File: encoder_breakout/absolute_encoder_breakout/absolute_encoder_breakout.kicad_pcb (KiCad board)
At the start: 2 copper layers, 14.3 x 9.7 mm, 2 parts

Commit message: Fix Breakout Board
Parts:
- moved U1 1.27 mm to (139.7, 75.2), turned to -90 degrees
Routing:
- net Net-(U1-OUT): track 5.43 -> 9.35 mm, vias 0 -> 1
- net Net-(U1-VDD3V3): track 5.74 -> 8.15 mm
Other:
- board size 14.3 x 9.7 mm -> 12 x 9.7 mm
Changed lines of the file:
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@@
 	(footprint "Package_SO:SOIC-8_3.9x4.9mm_P1.27mm"
 		(layer "F.Cu")
-		(at 138.43 75.15 180)
+		(at 139.7 75.184 -90)
 		(descr "SOIC, 8 Pin (JEDEC MS-012AA, https://www.analog.com/media/en/package-pcb-resources/package/pkg_pdf/soic_narrow-r/r_8.pdf), generated with kicad-footprint-generator ipc_gullwing_generator.py")
 		(tags "SOIC SO")
 		(property "Reference" "U1"
-			(at 0 -3.4 0)
-			(layer "F.SilkS")
+			(at 4.318 0 180)
+			(layer "F.SilkS")
+			(effects
+				(font
+					(size 0.635 0.635)
+					(thickness 0.15)
+				)
+			)
+		)
+		(property "Value" "~"
+			(at 0 3.4 90)
+			(layer "F.Fab")
 			(effects
 				(font
@@
 			)
 		)
-		(property "Value" "~"
-			(at 0 3.4 0)
-			(layer "F.Fab")
-			(effects
-				(font
-					(size 1 1)
-					(thickness 0.15)
-				)
-			)
-		)
 		(property "Datasheet" "https://look.ams-osram.com/m/7059eac7531a86fd/original/AS5600-DS000365.pdf"
-			(at 0 0 0)
+			(at 0 0 90)
 			(layer "F.Fab")
 			(hide yes)
@@
 		)
 		(property "Description" ""
-			(at 0 0 0)
+			(at 0 0 90)
 			(layer "F.Fab")
 			(hide yes)
@@
 		(fp_line
 			(start 0 2.56)
+			(end -1.95 2.56)
+			(stroke
+				(width 0.12)
+				(type solid)
+			)
+			(layer "F.SilkS")
+		)
+		(fp_line
+			(start 0 2.56)
 			(end 1.95 2.56)
 			(stroke
@@
 		)
 		(fp_line
-			(start 0 2.56)
-			(end -1.95 2.56)
+			(start 0 -2.56)
+			(end -1.95 -2.56)
 			(stroke
 				(width 0.12)
@@
 			(start 0 -2.56)
 			(end 1.95 -2.56)
-			(stroke
-				(width 0.12)
-				(type solid)
-			)
-			(layer "F.SilkS")
-		)
-		(fp_line
-			(start 0 -2.56)
-			(end -1.95 -2.56)
 			(stroke
 				(width 0.12)
@@
 		)
 		(fp_line
+			(start -2.2 2.7)
+			(end -2.2 2.46)
+			(stroke
+				(width 0.05)
+				(type solid)
+			)
+			(layer "F.CrtYd")
+		)
+		(fp_line
+			(start 2.2 2.7)
+			(end -2.2 2.7)
+			(stroke
+				(width 0.05)
+				(type solid)
+			)
+			(layer "F.CrtYd")
+		)
+		(fp_line
+			(start -3.7 2.46)
+			(end -3.7 -2.46)
+			(stroke
+				(width 0.05)
+				(type solid)
+			)
+			(layer "F.CrtYd")
+		)
+		(fp_line
+			(start -2.2 2.46)
+			(end -3.7 2.46)
+			(stroke
+				(width 0.05)
+				(type solid)
+			)
+			(layer "F.CrtYd")
+		)
+		(fp_line
+			(start 2.2 2.46)
+			(end 2.2 2.7)
+			(stroke
+				(width 0.05)
+				(type solid)
+			)
+			(layer "F.CrtYd")
+		)
+		(fp_line
 			(start 3.7 2.46)
 			(end 2.2 2.46)
@@
 		)
 		(fp_line
+			(start -3.7 -2.46)
+			(end -2.2 -2.46)
+			(stroke
+				(width 0.05)
+				(type solid)
+			)
+			(layer "F.CrtYd")
+		)
+		(fp_line
+			(start -2.2 -2.46)
+			(end -2.2 -2.7)
+			(stroke
+				(width 0.05)
+				(type solid)
+			)
+			(layer "F.CrtYd")
+		)
+		(fp_line
+			(start 2.2 -2.46)
+			(end 3.7 -2.46)
+			(stroke
+				(width 0.05)
+				(type solid)
+			)
+			(layer "F.CrtYd")
+		)
+		(fp_line
 			(start 3.7 -2.46)
 			(end 3.7 2.46)
@@
 		)
 		(fp_line
-			(start 2.2 2.7)
-			(end -2.2 2.7)
-			(stroke
-				(width 0.05)
-				(type solid)
-			)
-			(layer "F.CrtYd")
-		)
-		(fp_line
-			(start 2.2 2.46)
-			(end 2.2 2.7)
-			(stroke
-				(width 0.05)
-				(type solid)
-			)
-			(layer "F.CrtYd")
-		)
-		(fp_line
-			(start 2.2 -2.46)
-			(end 3.7 -2.46)
+			(start -2.2 -2.7)
+			(end 2.2 -2.7)
 			(stroke
 				(width 0.05)
@@
 			(start 2.2 -2.7)
 			(end 2.2 -2.46)
-			(stroke
-				(width 0.05)
-				(type solid)
-			)
-			(layer "F.CrtYd")
-		)
-		(fp_line
-			(start -2.2 2.7)
-			(end -2.2 2.46)
-			(stroke
-				(width 0.05)
-				(type solid)
-			)
-			(layer "F.CrtYd")
-		)
-		(fp_line
-			(start -2.2 2.46)
-			(end -3.7 2.46)
-			(stroke
-				(width 0.05)
-				(type solid)
-			)
-			(layer "F.CrtYd")
-		)
-		(fp_line
-			(start -2.2 -2.46)
-			(end -2.2 -2.7)
-			(stroke
-				(width 0.05)
-				(type solid)
-			)
-			(layer "F.CrtYd")
-		)
-		(fp_line
-			(start -2.2 -2.7)
-			(end 2.2 -2.7)
-			(stroke
-				(width 0.05)
-				(type solid)
-			)
-			(layer "F.CrtYd")
-		)
-		(fp_line
-			(start -3.7 2.46)
-			(end -3.7 -2.46)
-			(stroke
-				(width 0.05)
-				(type solid)
-			)
-			(layer "F.CrtYd")
-		)
-		(fp_line
-			(start -3.7 -2.46)
-			(end -2.2 -2.46)
 			(stroke
 				(width 0.05)
@@
 		)
 		(fp_text user "${REFERENCE}"
-			(at 0 0 0)
+			(at 0 0 90)
 			(layer "F.Fab")
 			(effects
@@
 		)
 		(pad "1" smd roundrect
-			(at -2.475 -1.905 180)
+			(at -2.475 -1.905 270)
 			(size 1.95 0.6)
 			(layers "F.Cu" "F.Mask" "F.Paste")
@@
 		)
 		(pad "2" smd roundrect
-			(at -2.475 -0.635 180)
+			(at -2.475 -0.635 270)
 			(size 1.95 0.6)
 			(layers "F.Cu" "F.Mask" "F.Paste")
@@
 		)
 		(pad "3" smd roundrect
-			(at -2.475 0.635 180)
+			(at -2.475 0.635 270)
 			(size 1.95 0.6)
 			(layers "F.Cu" "F.Mask" "F.Paste")
@@
 		)
 		(pad "4" smd roundrect
-			(at -2.475 1.905 180)
+			(at -2.475 1.905 270)
 			(size 1.95 0.6)
 			(layers "F.Cu" "F.Mask" "F.Paste")
@@
 		)
 		(pad "5" smd roundrect
-			(at 2.475 1.905 180)
+			(at 2.475 1.905 270)
 			(size 1.95 0.6)
 			(layers "F.Cu" "F.Mask" "F.Paste")
@@
 		)
 		(pad "6" smd roundrect
-			(at 2.475 0.635 180)
+			(at 2.475 0.635 270)
 			(size 1.95 0.6)
 			(layers "F.Cu" "F.Mask" "F.Paste")
@@
 		)
 		(pad "7" smd roundrect
-			(at 2.475 -0.635 180)
+			(at 2.475 -0.635 270)
 			(size 1.95 0.6)
 			(layers "F.Cu" "F.Mask" "F.Paste")
@@
 		)
 		(pad "8" smd roundrect
-			(at 2.475 -1.905 180)
+			(at 2.475 -1.905 270)
 			(size 1.95 0.6)
 			(layers "F.Cu" "F.Mask" "F.Paste")
@@
 	)
 	(gr_line
-		(start 134.322421 71.33042)
-		(end 134.322421 79.03758)
+		(start 136.652 71.33042)
+		(end 136.652 79.03758)
 		(stroke
 			(width 0.05)
@@
 	)
 	(gr_arc
-		(start 134.32242 71.33042)
-		(mid 134.62 70.612)
-		(end 135.33842 70.31442)
+		(start 136.651999 71.33042)
+		(mid 136.949579 70.612)
+		(end 137.667999 70.31442)
 		(stroke
 			(width 0.05)
@@
 	)
 	(gr_line
-		(start 135.3384 80.05358)
+		(start 137.668 80.05358)
 		(end 147.61758 80.05358)
 		(stroke
@@
 	(gr_line
 		(start 147.61758 70.314421)
-		(end 135.33842 70.31442)
+		(end 137.668 70.31442)
 		(stroke
 			(width 0.05)
@@
 	)
 	(gr_arc
-		(start 135.33842 80.05358)
-		(mid 134.62 79.756)
-		(end 134.32242 79.03758)
+		(start 137.667999 80.05358)
+		(mid 136.949579 79.756)
+		(end 136.651999 79.03758)
 		(stroke
 			(width 0.05)
@@
 	)
 	(gr_text "N"
-		(at 141.732 78.486 180)
+		(at 142.24 71.374 90)
 		(layer "F.SilkS")
 		(effects
@@
 	)
 	(gr_text "S"
-		(at 140.97 71.882 0)
+		(at 138.176 71.374 90)
 		(layer "F.SilkS")
 		(effects
@@
 	)
 	(gr_text "Encoder Breakout\nMars Rover Design Team\nMissouri S&T, 2026\nLucas Boeyink\nTyler Hughes"
-		(at 144.526 77.216 0)
+		(at 147.066 77.216 0)
 		(layer "B.SilkS")
 		(effects
@@
 	)
 	(segment
-		(start 143.349 74.515)
-		(end 144.049 75.215)
-		(width 0.2)
+		(start 139.192 75.184)
+		(end 139.192 72.836)
+		(width 0.254)
 		(layer "F.Cu")
 		(net 1)
 	)
 	(segment
-		(start 140.905 74.515)
-		(end 143.349 74.515)
-		(width 0.2)
+		(start 139.192 72.836)
+		(end 139.065 72.709)
+		(width 0.254)
 		(layer "F.Cu")
 		(net 1)
 	)
+	(via
+		(at 139.192 75.184)
+		(size 0.6)
+		(drill 0.3)
+		(layers "F.Cu" "B.Cu")
+		(net 1)
+	)
 	(segment
-		(start 144.049 75.215)
-		(end 146.05 75.215)
-		(width 0.2)
-		(layer "F.Cu")
+		(start 146.05 75.215)
+		(end 139.223 75.215)
+		(width 0.254)
+		(layer "B.Cu")
 		(net 1)
 	)
 	(segment
-		(start 144.017 77.215)
+		(start 143.866001 77.215)
 		(end 146.05 77.215)
-		(width 0.2)
+		(width 0.254)
 		(layer "F.Cu")
 		(net 2)
 	)
 	(segment
-		(start 142.587 75.785)
-		(end 144.017 77.215)
-		(width 0.2)
+		(start 140.335 72.709)
+		(end 140.335 73.683999)
+		(width 0.254)
 		(layer "F.Cu")
 		(net 2)
 	)
 	(segment
-		(start 140.905 75.785)
-		(end 142.587 75.785)
-		(width 0.2)
+		(start 140.335 73.683999)
+		(end 143.866001 77.215)
+		(width 0.254)
 		(layer "F.Cu")
 		(net 2)

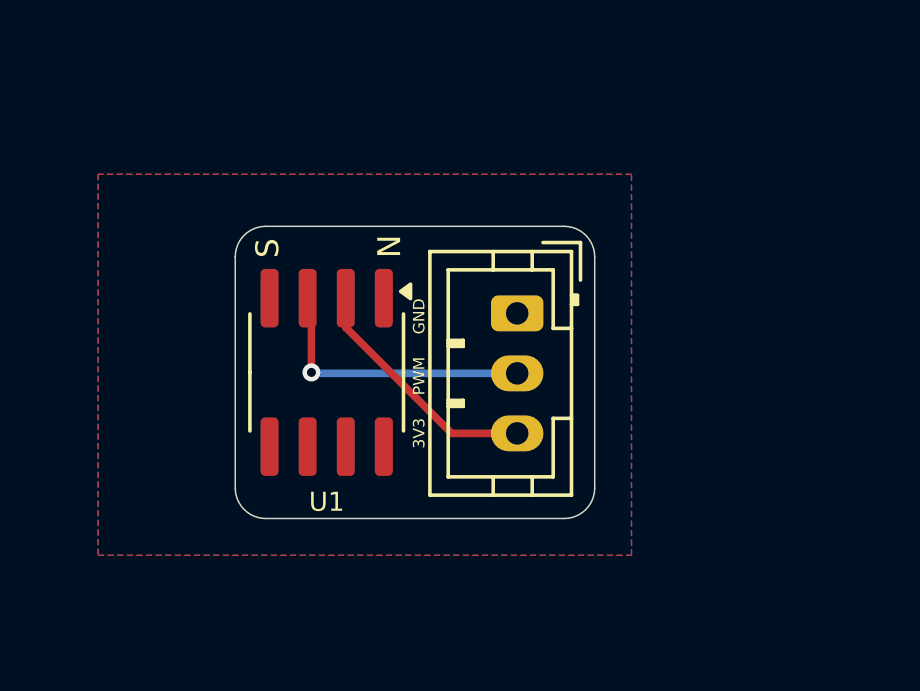
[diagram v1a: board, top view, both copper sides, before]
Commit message: Fix Breakout Schematic and Layout
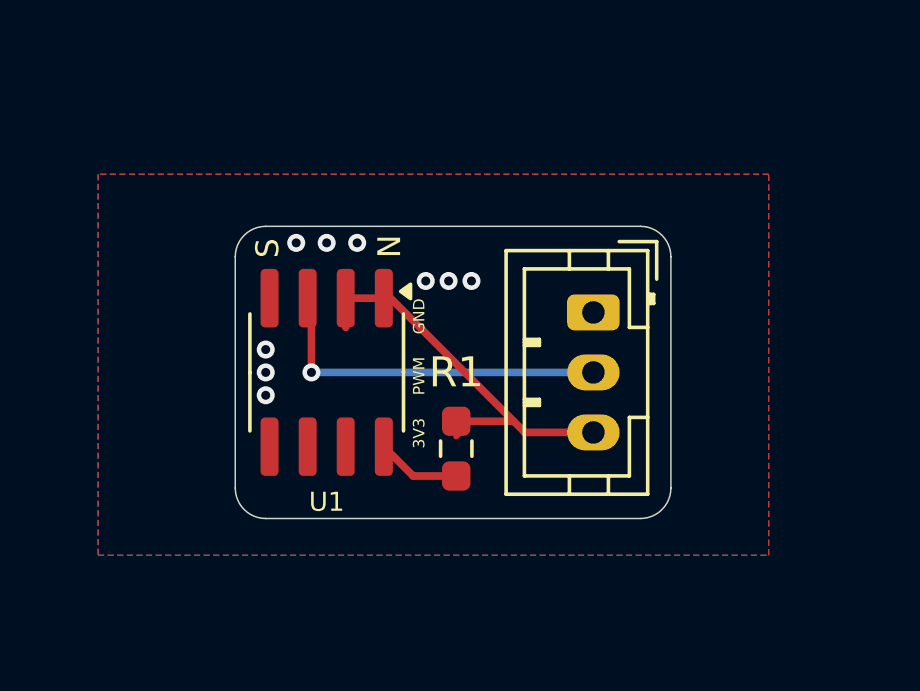
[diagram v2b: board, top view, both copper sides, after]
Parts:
- added R1: 0, Resistor_SMD:R_0603_1608Metric_Pad0.98x0.95mm_HandSolder, F.Cu at (144.0, 77.7)
- moved Conn1 2.54 mm to (148.6, 73.2)
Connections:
- U1 pad 1: unconnected-(U1-VDD5V-Pad1) -> Net-(U1-VDD3V3)
- U1 pad 5: unconnected-(U1-PGO-Pad5) -> GND
- U1 pad 8: unconnected-(U1-DIR-Pad8) -> Net-(U1-DIR)
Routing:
- net Net-(U1-VDD3V3): track 8.15 -> 13.7 mm
- net Net-(U1-DIR): track 0.00 -> 2.82 mm
- net Net-(U1-OUT): track 9.35 -> 11.9 mm
- net GND: vias 0 -> 9
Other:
- board size 12 x 9.7 mm -> 14.5 x 9.7 mm

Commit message: Final Encoder Breakout
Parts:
- removed Conn1: Molex_SL_03, Connector_JST:JST_PH_B3B-PH-K_1x03_P2.00mm_Vertical
- added C1: 10uF, Capacitor_SMD:C_0603_1608Metric_Pad1.08x0.95mm_HandSolder, B.Cu at (139.3, 75.7)
- added J1: Conn_01x03_Pin, Connector_JST:JST_PH_S3B-PH-K_1x03_P2.00mm_Horizontal, B.Cu at (143.9, 72.7)
- R1: moved to B.Cu
- moved R1 6.57 mm to (139.3, 73.2), turned to 180 degrees
- moved U1 0.69 mm to (139.3, 74.6), turned to 90 degrees
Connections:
- U1 pad 5: GND -> unconnected-(U1-PGO-Pad5)
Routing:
- net Net-(J1-Pin_2): track 11.9 -> 5.34 mm, vias 1 -> 0
- net Net-(J1-Pin_1): track 13.7 -> 19.7 mm
- net Net-(U1-DIR): track 2.82 -> 1.84 mm, vias 0 -> 1
- net GND: vias 9 -> 1
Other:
- board size 14.5 x 9.7 mm -> 10.2 x 9.1 mm
- board text added: "_"
